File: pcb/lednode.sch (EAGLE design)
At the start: 50 parts, among them Q1 AO3402, Q2 AO3402, Q3 AO3402, Q4 AO3402, Q5 AO3402, Q6 AO3402

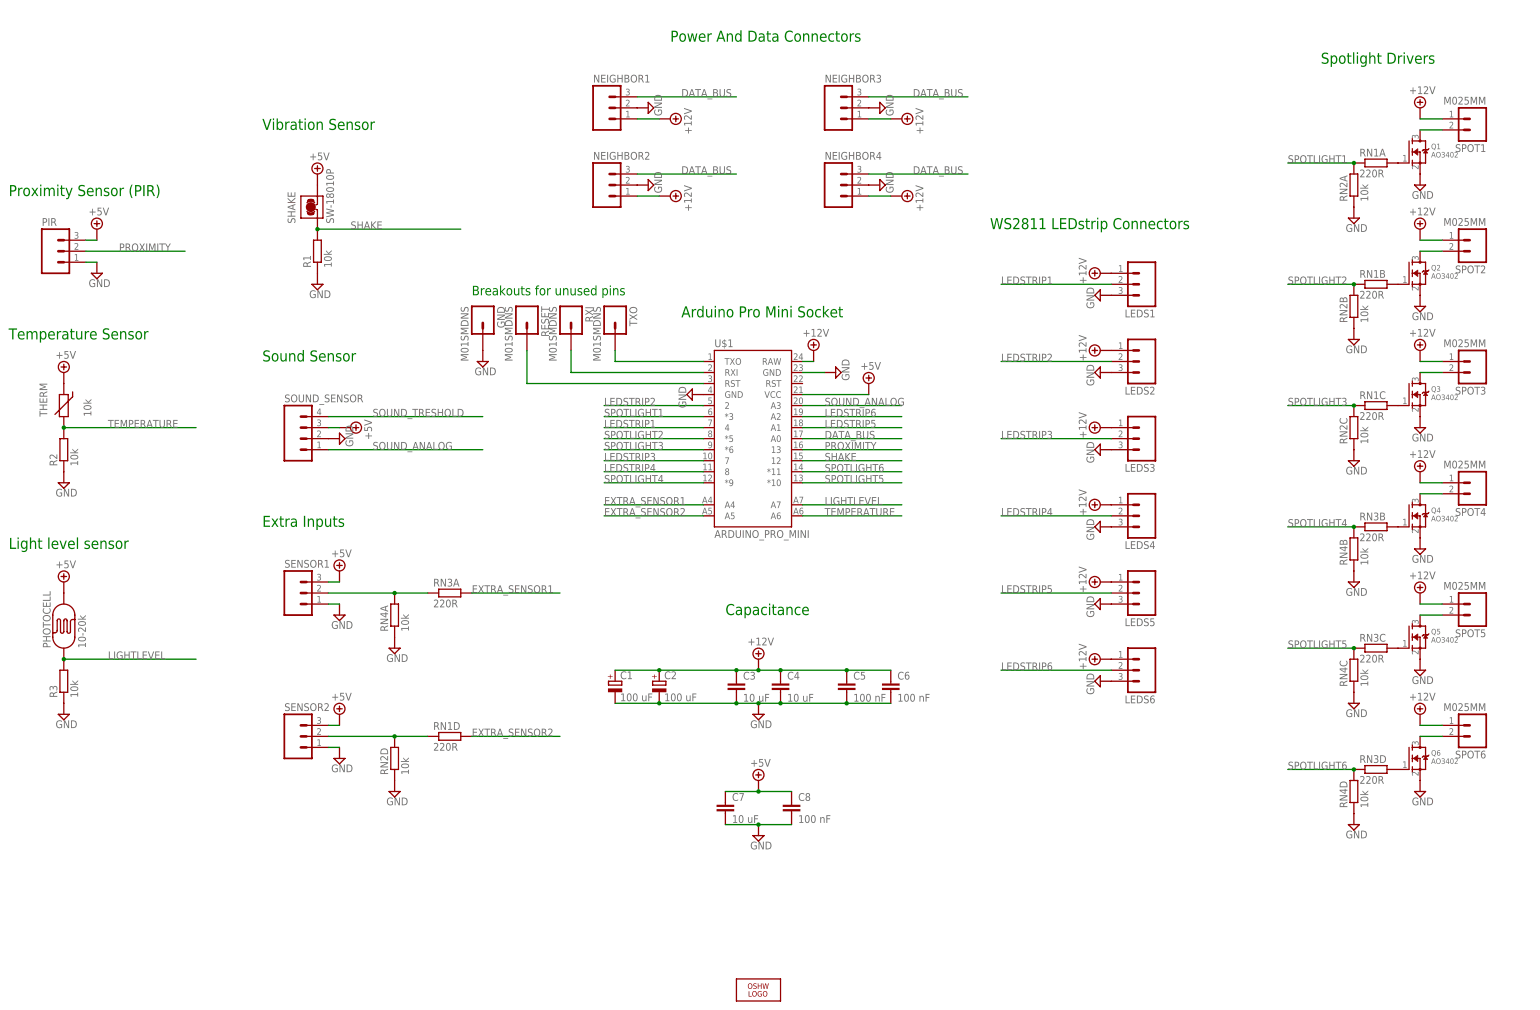
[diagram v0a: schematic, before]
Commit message: Removed old versions of the lednode and removed version numbers from the filenames.
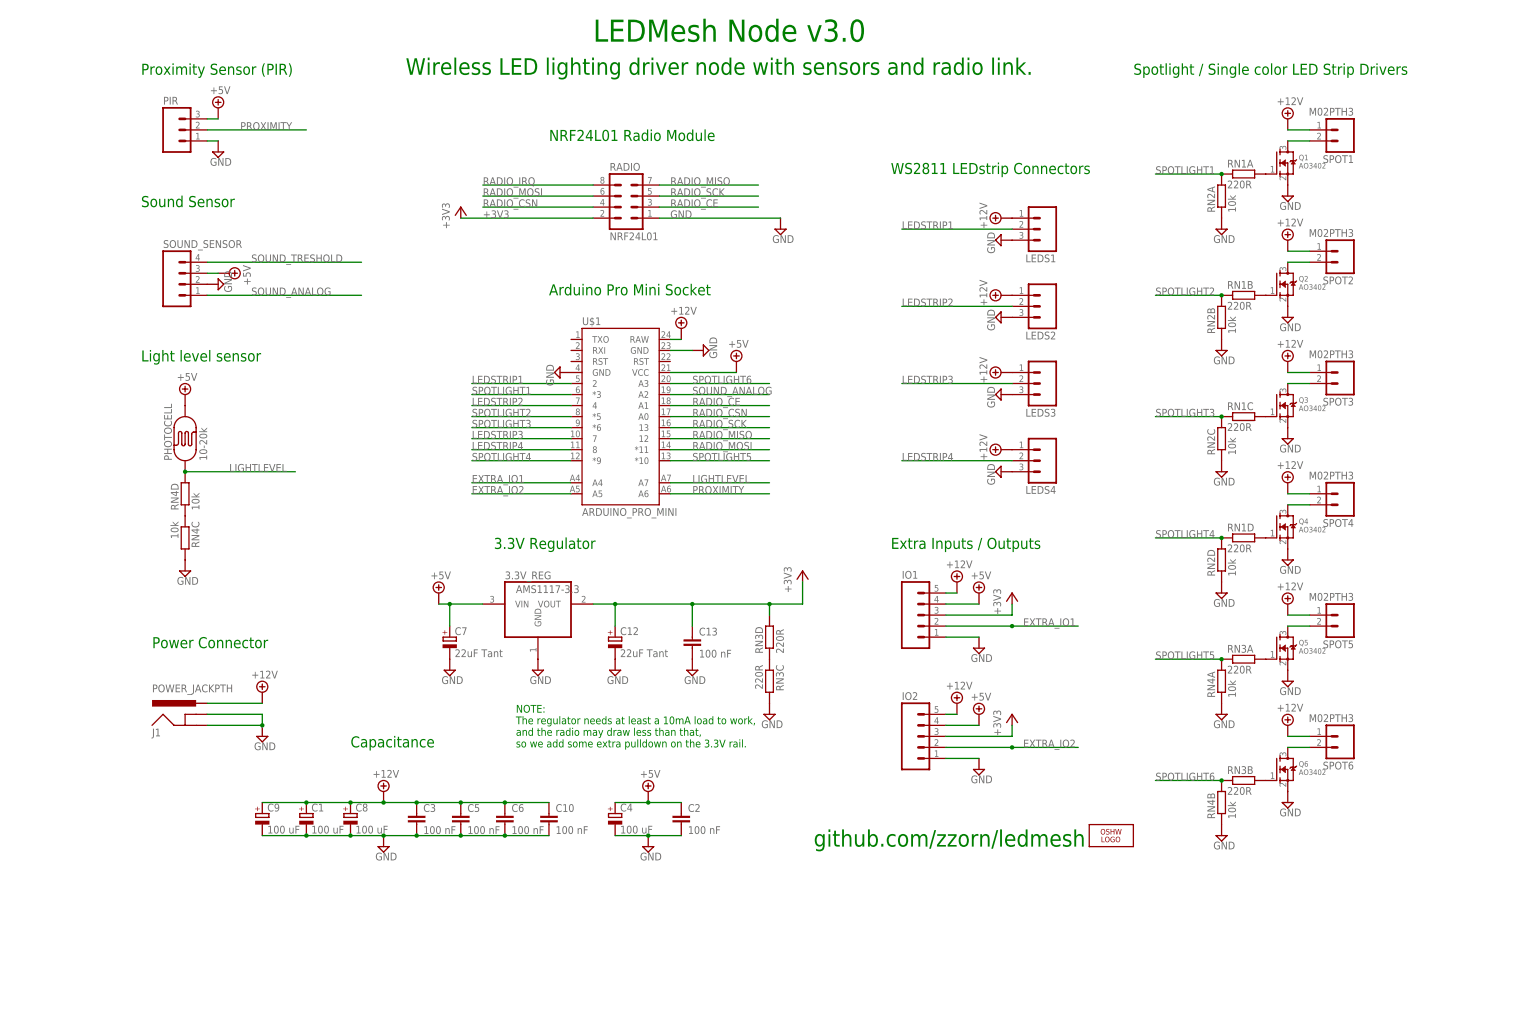
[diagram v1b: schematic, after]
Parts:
- removed GND, RESET, RXI, TXO: M01SMDNS, SparkFun-Connectors:M01SMDNS
- removed LEDS5, LEDS6: (no value), SparkFun-Connectors:M03LONGPADS
- removed NEIGHBOR1, NEIGHBOR2, NEIGHBOR3, NEIGHBOR4: (no value), SparkFun-Connectors:M03-SCREW-5MM
- removed R1, R2, R3: 10k, rcl:R-EU_R0805
- removed SENSOR1, SENSOR2: (no value), SparkFun-Connectors:M03PTH
- removed SHAKE: SW-18010P, sensor-comus-group:CM4400
- removed THERM: 10k, discrete-fixed-thermistor-silk:THERMISTOR_R-7,5
- added 3.3V_REG: AMS1117-3.3, burr-brown:REG1117
- added C10, C13: 100 nF, rcl:C-EUC0805
- added C12: 22uF Tant, rcl:CPOL-EUSMCA
- added C9: 100 uF, rcl:CPOL-EUE2.5-6
- added IO1, IO2: (no value), SparkFun-Connectors:M05PTH
- added J1: POWER_JACKPTH, SparkFun-Connectors:POWER_JACKPTH
- added RADIO: NRF24L01, con-lstb:MA04-2
- C1: device rcl:CPOL-EUE3.5-10 -> rcl:CPOL-EUE2.5-6
- C2: value 100 uF -> 100 nF; device rcl:CPOL-EUE3.5-10 -> rcl:C-EUC0805
- C3: value 10 uF -> 100 nF; device rcl:C-EUC1206 -> rcl:C-EUC0805
- C4: value 10 uF -> 100 uF; device rcl:C-EUC1206 -> rcl:CPOL-EUE2.5-6
- C7: value 10 uF -> 22uF Tant; device rcl:C-EUC1206 -> rcl:CPOL-EUSMCA
- C8: value 100 nF -> 100 uF; device rcl:C-EUC0805 -> rcl:CPOL-EUE2.5-6
- SPOT1, SPOT2, SPOT3, SPOT4, SPOT5, SPOT6: value M025MM -> M02PTH3; device SparkFun-Connectors:M025MM -> SparkFun-Connectors:M02PTH3
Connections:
- removed net DATA_BUS: NEIGHBOR1.3, NEIGHBOR2.3, NEIGHBOR3.3, NEIGHBOR4.3, U$1.A0
- removed net EXTRA_SENSOR1: RN3A.2, U$1.A4
- removed net EXTRA_SENSOR2: RN1D.2, U$1.A5
- removed net LEDSTRIP5: LEDS5.2, U$1.A1
- removed net LEDSTRIP6: LEDS6.2, U$1.A2
- removed net N$15: RXI.1, U$1.RXI
- removed net N$16: RESET.1, U$1.RST
- removed net SENSOR1: RN3A.1, RN4A.2, SENSOR1.2
- removed net SHAKE: R1.2, SHAKE.1, U$1.12
- removed net TEMPERATURE: R2.2, THERM.2, U$1.A6
- new net +3V3: 3.3V_REG.VOUT, C12.+, C13.1, IO1.3, IO2.3, RADIO.2, RN3D.2
- new net EXTRA_IO1: IO1.2, U$1.A4
- new net EXTRA_IO2: IO2.2, U$1.A5
- new net RADIO_CE: RADIO.3, U$1.A1
- new net RADIO_CSN: RADIO.4, U$1.A0
- new net RADIO_IRQ: RADIO.8
- new net RADIO_MISO: RADIO.7, U$1.12
- new net RADIO_MOSI: RADIO.6, U$1.*11
- new net RADIO_SCK: RADIO.5, U$1.13
- net +12V: now also C10.1, C8.+, C9.+, IO1.5, IO2.5, J1.PWR; no longer C2.+, C4.1, LEDS5.1, LEDS6.1, NEIGHBOR1.1, NEIGHBOR2.1, NEIGHBOR3.1, NEIGHBOR4.1
- net +5V: now also 3.3V_REG.VIN, C2.1, C4.+, C7.+, IO1.4, IO2.4; no longer C7.1, C8.1, SENSOR1.3, SENSOR2.3, SHAKE.2, THERM.1
- net GND: now also 3.3V_REG.GND, C10.2, C12.-, C13.2, C2.2, C4.-, C7.-, C8.-, C9.-, IO1.1, IO2.1, J1.GND, J1.GNDBREAK, RADIO.1, RN3C.2, RN4C.2; no longer C2.-, C4.2, C7.2, C8.2, GND.1, LEDS5.3, LEDS6.3, NEIGHBOR1.2, NEIGHBOR2.2, NEIGHBOR3.2, NEIGHBOR4.2, R1.1, R2.1, R3.1, RN4C.1, RN4D.1, SENSOR1.1, SENSOR2.1
- net LEDSTRIP1: now also U$1.2; no longer U$1.4
- net LEDSTRIP2: now also U$1.4; no longer U$1.2
- net LIGHTLEVEL: now also RN4D.2; no longer R3.2
- net N$10: now also RN3A.2; no longer RN3C.2
- net N$12: now also RN4C.1, RN4D.1; no longer Q6.G, RN3D.2
- net N$13: now also Q6.G, RN3B.2; no longer RN1D.1, RN2D.2, SENSOR2.2
- net N$14: now also RN3C.1, RN3D.1; no longer TXO.1, U$1.TXO
- net N$8: now also RN1D.2; no longer RN3B.2
- net PROXIMITY: now also U$1.A6; no longer U$1.13
- net SOUND_ANALOG: now also U$1.A2; no longer U$1.A3
- net SPOTLIGHT4: now also RN1D.1, RN2D.2; no longer RN3B.1, RN4B.2
- net SPOTLIGHT5: now also RN3A.1, RN4A.2; no longer RN3C.1, RN4C.2
- net SPOTLIGHT6: now also RN3B.1, RN4B.2, U$1.A3; no longer RN3D.1, RN4D.2, U$1.*11
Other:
- note added: "3.3V Regulator"
- note added: "Extra Inputs / Outputs"
- note added: "LEDMesh Node v3.0"
- note added: "NOTE: The regulator needs at least a 10mA load to work, and the radio may draw less than that, so we add some extra pulldown on the 3.3V rail."
- note added: "NRF24L01 Radio Module"
- note added: "Power Connector"
- note added: "Spotlight / Single color LED Strip Drivers"
- note added: "Wireless LED lighting driver node with sensors and radio link."
- note added: "github.com/zzorn/ledmesh"
- note removed: "Breakouts for unused pins"
- note removed: "Extra Inputs"
- note removed: "Power And Data Connectors"
- note removed: "Spotlight Drivers"
- note removed: "Temperature Sensor"
- note removed: "Vibration Sensor"
- moved on the sheet: C1, C3, C5, C6, LEDS1, LEDS2, LEDS3, LEDS4, PHOTOCELL, PIR, Q1, Q2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
